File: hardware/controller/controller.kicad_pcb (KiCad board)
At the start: 2 copper layers, 30 x 100 mm, 33 parts, among them J1 DC_12V_IN, J2 HDD_POWER_OUT, J3 470531000, J4 470531000, J5 Conn_01x07, Q1 2N3904, Q2 2N3904, U1 TSR0.5-2450, U2 XIAO-RP2350-SMD, U3 INA228, U4 74HC4051

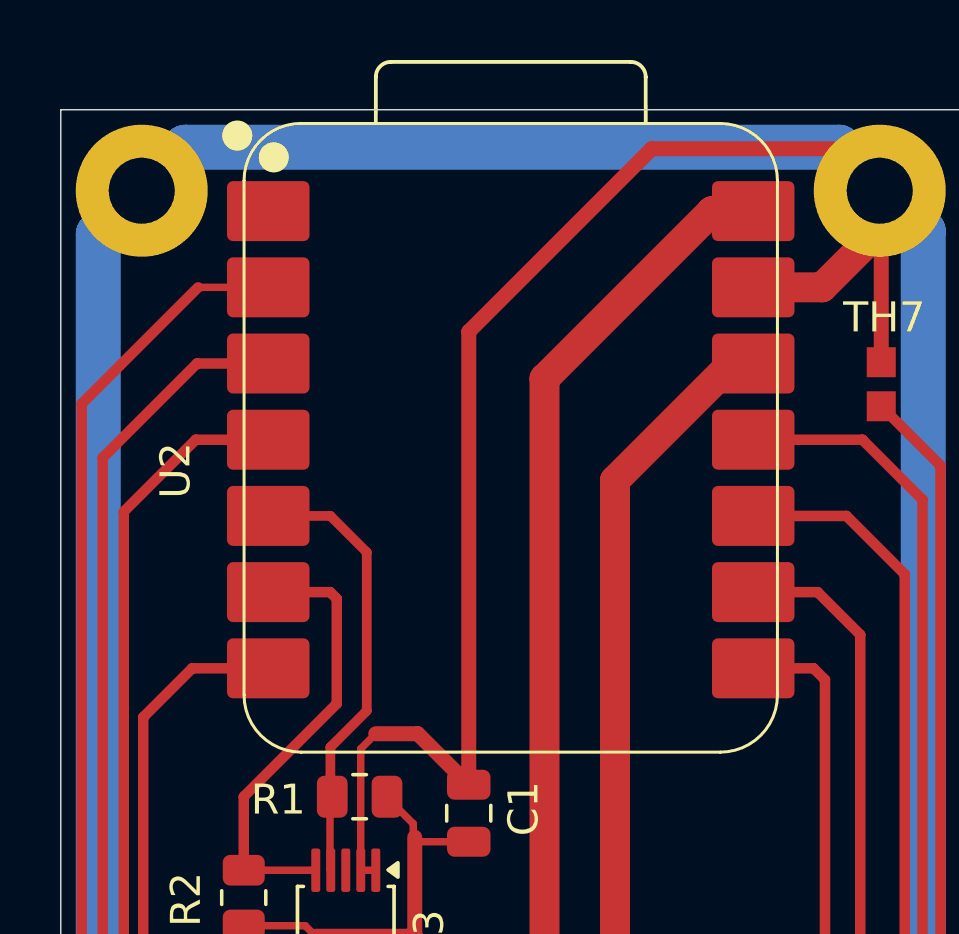
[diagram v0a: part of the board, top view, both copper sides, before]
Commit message: updated DRC
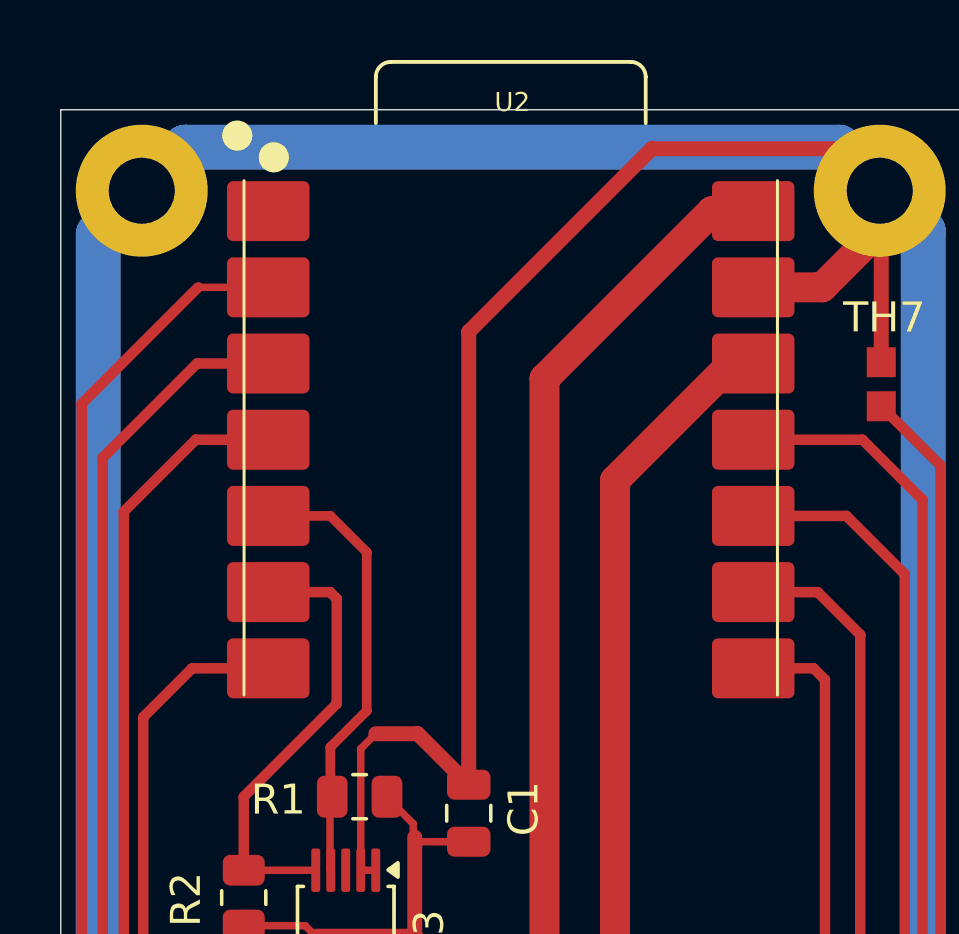
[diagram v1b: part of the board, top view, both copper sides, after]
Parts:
- U2: value XIAO-RP2350-SMD -> XIAO-RP2350-no-underside; footprint Seeed_Studio_XIAO_Series:XIAO-RP2350-SMD -> XIAO_RP2350:XIAO-RP2350-no-underside
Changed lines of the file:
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@@
 		(capping no)
 		(filling no)
-		(zone_defaults)
 		(pcbplotparams
 			(layerselection 0x00000000_00000000_55555555_5755f5ff)
@@
 		(embedded_fonts no)
 	)
-	(footprint "Seeed_Studio_XIAO_Series:XIAO-RP2350-SMD"
+	(footprint "XIAO_RP2350:XIAO-RP2350-no-underside"
 		(layer "F.Cu")
 		(at 65.5 60 90)
 		(property "Reference" "U2"
-			(at -1.025 -11.175 90)
+			(at 11.25 0.05 0)
 			(unlocked yes)
 			(layer "F.SilkS")
 			(effects
 				(font
-					(size 1 1)
-					(thickness 0.15)
+					(size 0.635 0.635)
+					(thickness 0.1016)
 				)
 			)
 		)
-		(property "Value" "XIAO-RP2350-SMD"
+		(property "Value" "XIAO-RP2350-no-underside"
 			(at -11.5 0 0)
 			(unlocked yes)
@@
 		(sheetname "/")
 		(sheetfile "controller.kicad_sch")
-		(units
-			(unit
-				(name "A")
-				(pins "1" "2" "3" "4" "5" "6" "7" "15" "16" "17" "18" "23" "24" "25"
-					"29" "26" "30" "27" "28" "14" "13" "12" "11" "10" "9" "8" "22" "21"
-					"20" "19"
-				)
-			)
-		)
 		(attr smd)
 		(duplicate_pad_numbers_are_jumpers no)
@@
 		)
 		(fp_line
-			(start -10.414 -6.985)
-			(end -10.414 6.985)
-			(stroke
-				(width 0.1)
-				(type solid)
-			)
-			(layer "F.SilkS")
-		)
-		(fp_line
 			(start 10.553 -4.498)
 			(end 12.094284 -4.497284)
@@
 		)
 		(fp_line
-			(start 10.541 6.985)
-			(end 10.541 -6.985)
-			(stroke
-				(width 0.1)
-				(type solid)
-			)
-			(layer "F.SilkS")
-		)
-		(fp_line
 			(start -8.509 8.89)
 			(end 8.636 8.89)
@@
 		)
 		(fp_arc
-			(start 8.64 -8.89)
-			(mid 9.987038 -8.332038)
-			(end 10.545 -6.985)
-			(stroke
-				(width 0.1)
-				(type solid)
-			)
-			(layer "F.SilkS")
-		)
-		(fp_arc
-			(start -10.414 -6.985)
-			(mid -9.856038 -8.332038)
-			(end -8.509 -8.89)
-			(stroke
-				(width 0.1)
-				(type solid)
-			)
-			(layer "F.SilkS")
-		)
-		(fp_arc
 			(start 12.094284 -4.497284)
 			(mid 12.447619 -4.350707)
@@
 			(layer "F.SilkS")
 		)
-		(fp_arc
-			(start 10.541 6.985)
-			(mid 9.983038 8.332038)
-			(end 8.636 8.89)
-			(stroke
-				(width 0.1)
-				(type solid)
-			)
-			(layer "F.SilkS")
-		)
-		(fp_arc
-			(start -8.509 8.89)
-			(mid -9.856038 8.332038)
-			(end -10.414 6.985)
-			(stroke
-				(width 0.1)
-				(type solid)
-			)
-			(layer "F.SilkS")
-		)
 		(fp_circle
 			(center 10.137012 -9.116012)
@@
 			(layer "F.CrtYd")
 		)
+		(fp_line
+			(start -10.414 -6.985)
+			(end -10.414 6.985)
+			(stroke
+				(width 0.1)
+				(type solid)
+			)
+			(layer "F.Fab")
+		)
+		(fp_line
+			(start 10.541 6.985)
+			(end 10.541 -6.985)
+			(stroke
+				(width 0.1)
+				(type solid)
+			)
+			(layer "F.Fab")
+		)
 		(fp_rect
 			(start -10.41 -8.9)
@@
 			(layer "F.Fab")
 		)
+		(fp_arc
+			(start 8.64 -8.89)
+			(mid 9.987038 -8.332038)
+			(end 10.545 -6.985)
+			(stroke
+				(width 0.1)
+				(type solid)
+			)
+			(layer "F.Fab")
+		)
+		(fp_arc
+			(start -10.414 -6.985)
+			(mid -9.856038 -8.332038)
+			(end -8.509 -8.89)
+			(stroke
+				(width 0.1)
+				(type solid)
+			)
+			(layer "F.Fab")
+		)
+		(fp_arc
+			(start 10.541 6.985)
+			(mid 9.983038 8.332038)
+			(end 8.636 8.89)
+			(stroke
+				(width 0.1)
+				(type solid)
+			)
+			(layer "F.Fab")
+		)
+		(fp_arc
+			(start -8.509 8.89)
+			(mid -9.856038 8.332038)
+			(end -10.414 6.985)
+			(stroke
+				(width 0.1)
+				(type solid)
+			)
+			(layer "F.Fab")
+		)
 		(fp_circle
 			(center 9.357 -7.961)
@@
 	)
 	(segment
-		(start 59.536396 81.2)
-		(end 60.5 80.236396)
-		(width 0.25)
-		(layer "F.Cu")
-		(net "Net-(U3-Vin-)")
-	)
-	(segment
-		(start 55.75 82.1875)
-		(end 56.7375 81.2)
-		(width 0.25)
-		(layer "F.Cu")
-		(net "Net-(U3-Vin-)")
-	)
-	(segment
-		(start 57.8875 82.1875)
-		(end 58.1 82.4)
-		(width 0.25)
-		(layer "F.Cu")
-		(net "Net-(U3-Vin-)")
-	)
-	(segment
-		(start 60.5 80.236396)
-		(end 60.5 78.65)
-		(width 0.25)
-		(layer "F.Cu")
-		(net "Net-(U3-Vin-)")
-	)
-	(segment
-		(start 56.7375 81.2)
-		(end 59.536396 81.2)
-		(width 0.25)
-		(layer "F.Cu")
-		(net "Net-(U3-Vin-)")
-	)
-	(segment
-		(start 55.75 82.1875)
-		(end 57.8875 82.1875)
-		(width 0.5)
-		(layer "F.Cu")
-		(net "Net-(U3-Vin-)")
-	)
-	(segment
 		(start 59.308578 80.65)
 		(end 60 79.958578)
@@
 	)
 	(segment
+		(start 59.536396 81.2)
+		(end 60.5 80.236396)
+		(width 0.25)
+		(layer "F.Cu")
+		(net "Net-(U3-Vin-)")
+	)
+	(segment
+		(start 55.75 82.1875)
+		(end 56.7375 81.2)
+		(width 0.25)
+		(layer "F.Cu")
+		(net "Net-(U3-Vin-)")
+	)
+	(segment
+		(start 57.8875 82.1875)
+		(end 58.1 82.4)
+		(width 0.25)
+		(layer "F.Cu")
+		(net "Net-(U3-Vin-)")
+	)
+	(segment
+		(start 60.5 80.236396)
+		(end 60.5 78.65)
+		(width 0.25)
+		(layer "F.Cu")
+		(net "Net-(U3-Vin-)")
+	)
+	(segment
+		(start 56.7375 81.2)
+		(end 59.536396 81.2)
+		(width 0.25)
+		(layer "F.Cu")
+		(net "Net-(U3-Vin-)")
+	)
+	(segment
+		(start 55.75 82.1875)
+		(end 57.8875 82.1875)
+		(width 0.5)
+		(layer "F.Cu")
+		(net "Net-(U3-Vin-)")
+	)
+	(segment
